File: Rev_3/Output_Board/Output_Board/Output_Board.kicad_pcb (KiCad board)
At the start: 2 copper layers, 28.5 x 59 mm, 5 parts, among them J1 6, J2 6, J3 6

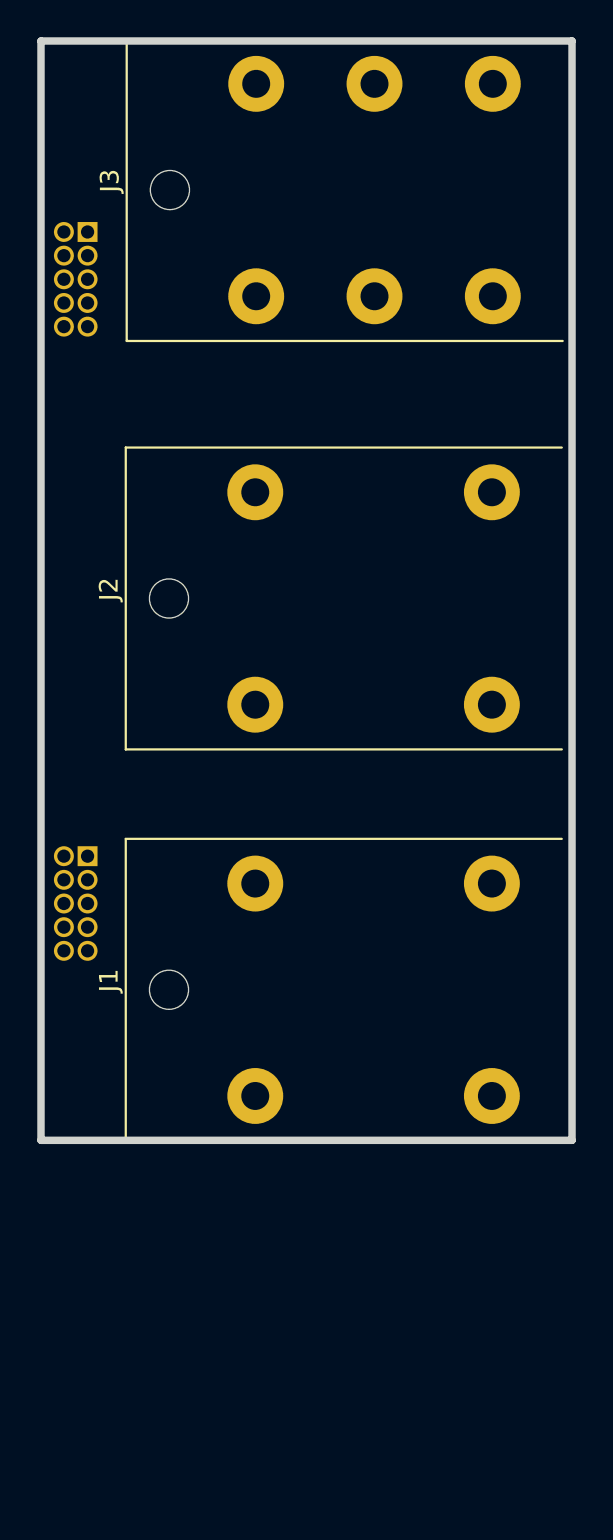
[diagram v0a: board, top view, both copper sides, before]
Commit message: Added analog board back, switched to Jacks on Bottom
Added analog board mezzanine back to fit everything. Finalized decision on jack boards; jacks on bottom, wire to board connectors between jack boards and digital board. Tentative board outlines defined and scoped out component placement.
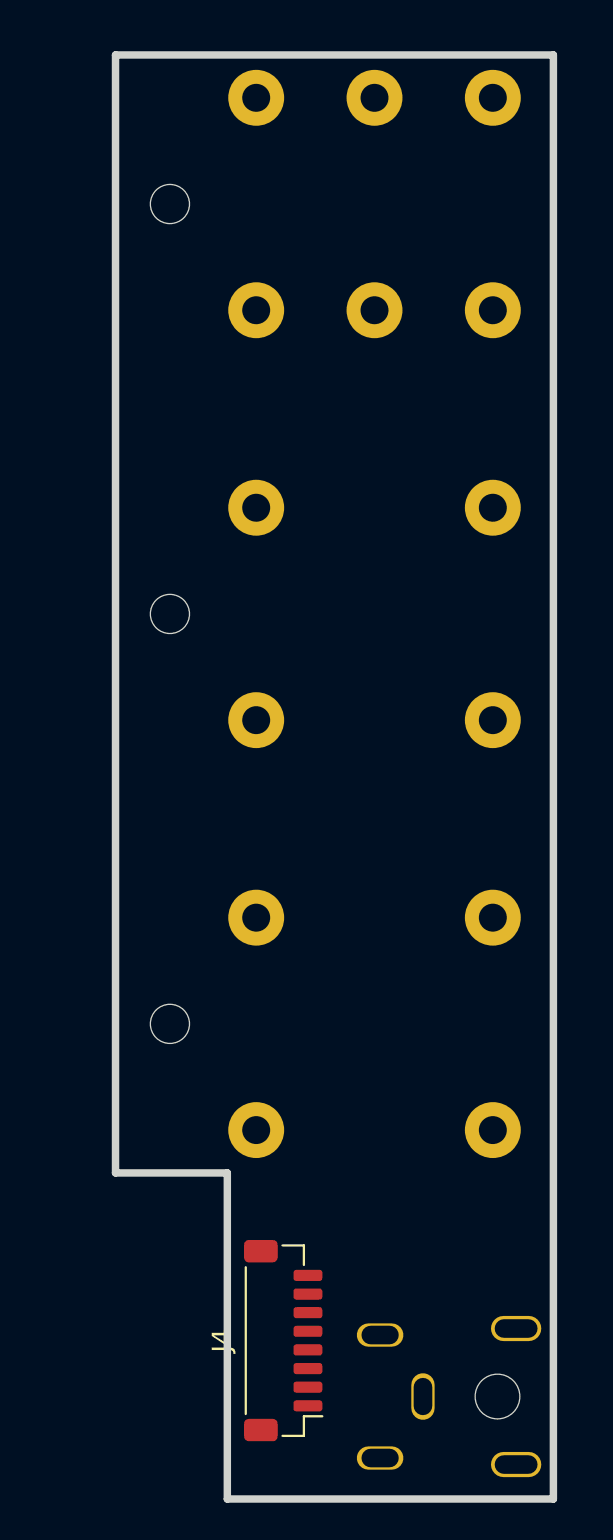
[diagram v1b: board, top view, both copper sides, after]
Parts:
- removed REF** (x2): CONN_SAMTEC_FTS-105, g-con:CONN_SAMTEC_FTS-105
- added J4: 8, Connector_JST:JST_SH_BM08B-SRSS-TB_1x08-1MP_P1.00mm_Vertical, F.Cu at (94.0, 149.0)
- added J5: 1, g-con:BarrelJack_CUI_PJ-047AH, B.Cu at (103.8, 152.0)
- J1, J2, J3: moved to B.Cu
- moved J1 1.83 mm to (109.5, 132.0)
- moved J2 0.83 mm to (109.5, 110.0)
- moved J3 0.75 mm to (109.5, 88.0)
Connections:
- J3 pad S: DGND -> GNDD
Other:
- board size 28.5 x 59 mm -> 23.5 x 77.5 mm
